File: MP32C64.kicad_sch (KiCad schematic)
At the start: 15 parts, among them CN2 C64_CASS_PORT, J1 Conn_Coaxial, SW1 SW_SPDT, U1 4069

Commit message: Almost ready
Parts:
- removed J1: Conn_Coaxial, symbol Connector:Conn_Coaxial
- added CN1: AUDIO_IN, MP32C64:SWITCHCRAFT_PJRAN1X1U01X, symbol PJRAN1X1U01X:PJRAN1X1U01X
- R1, R2, R3, R4, R5, R6, R7, R8: footprint Resistor_THT:R_Axial_DIN0207_L6.3mm_D2.5mm_P7.62mm_Horizontal -> Resistor_THT:R_Axial_DIN0207_L6.3mm_D2.5mm_P10.16mm_Horizontal
- SW1: value SW_SPDT -> SW_INVERT
- U1: value 4069 -> CD4069
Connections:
- net GND: now also CN1.1
- net at C1.1, R1.2: now also CN1.2
- no-connect marks 1 -> 2
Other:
- moved on the sheet: C1, R1

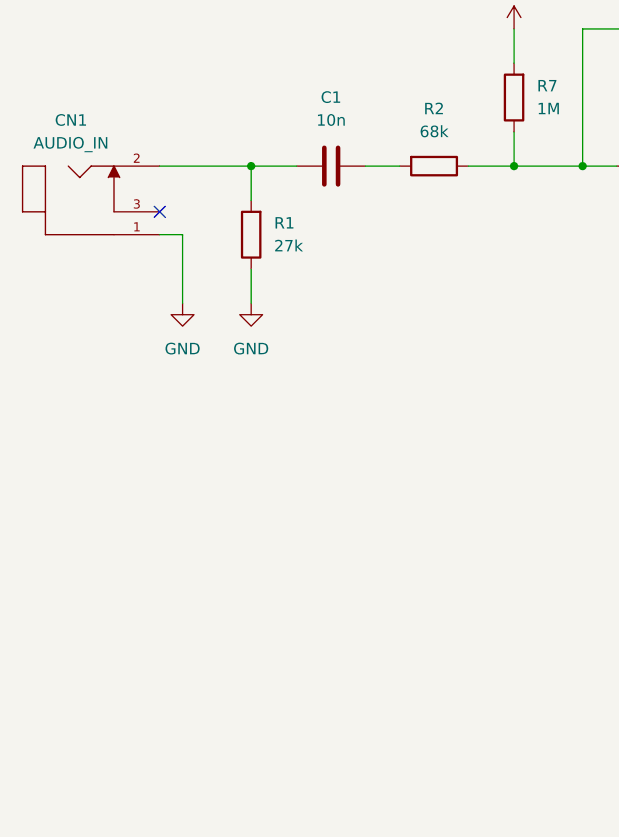
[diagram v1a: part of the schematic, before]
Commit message: Add dual support for RCA/3.5" jack connector
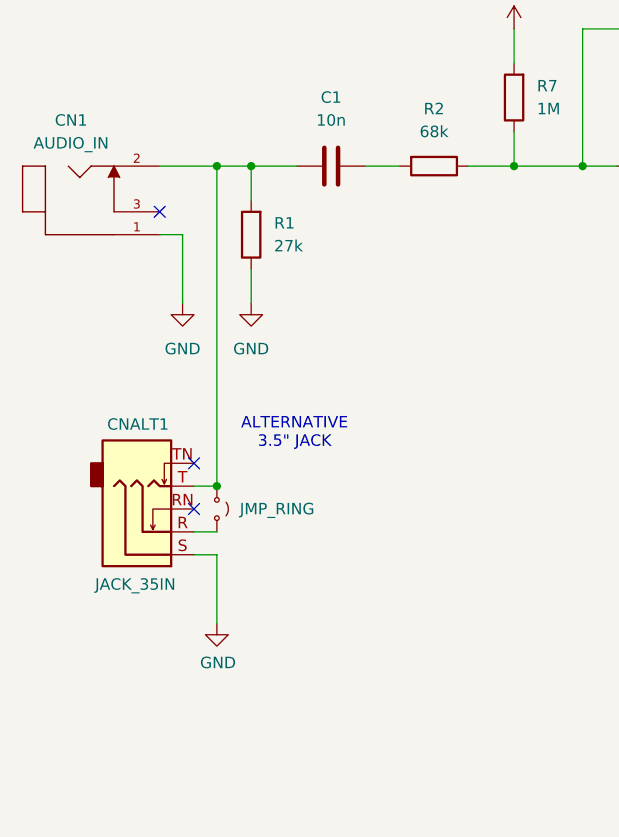
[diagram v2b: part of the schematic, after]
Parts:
- added CNALT1: JACK_35IN, MP32C64:AudioJack_SJ1-3525N, symbol Connector_Audio:AudioJack3_SwitchTR
- added JP1: JMP_RING, Jumper:SolderJumper-2_P1.3mm_Open_RoundedPad1.0x1.5mm, symbol Jumper:Jumper_2_Small_Open
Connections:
- net GND: now also CNALT1.S
- net at C1.1, CN1.2, R1.2: now also CNALT1.T, JP1.1 (A)
- new net: CNALT1.R, JP1.2 (B)
- no-connect marks 2 -> 4
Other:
- note added: "ALTERNATIVE 3.5" JACK"

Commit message: Add license, etc.
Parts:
- removed JP1: JMP_RING, Jumper:SolderJumper-2_P1.3mm_Open_RoundedPad1.0x1.5mm, symbol Jumper:Jumper_2_Small_Open
- added V0: LICENSE, MP32C64:cc_by_nc_sa_small, symbol void:Void
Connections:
- no-connect marks 4 -> 5
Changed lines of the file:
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@@
 		(company "SukkoPera")
 		(comment 1 "Audio Device to C64 Datassette Adapter")
-		(comment 2 "https://www.c64-wiki.com/wiki/MP32C64")
+		(comment 2 "https://github.com/SukkoPera/MP32C64")
 		(comment 3 "Original design by Kopsec")
 	)
@@
 	)
 	(junction
-		(at 34.29 91.44)
-		(diameter 0)
-		(color 0 0 0 0)
-	)
-	(junction
 		(at 67.31 55.88)
 		(diameter 0)
@@
 	)
 	(no_connect
+		(at 31.75 96.52)
+	)
+	(no_connect
 		(at 31.75 88.9)
 	)
@@
 		(pts
 			(xy 261.62 66.04) (xy 259.08 66.04)
-		)
-		(stroke
-			(width 0)
-			(type default)
-		)
-	)
-	(wire
-		(pts
-			(xy 31.75 96.52) (xy 34.29 96.52)
 		)
 		(stroke
@@
 	)
 	(symbol
+		(lib_id "void:Void")
+		(at 266.7 161.29 0)
+		(unit 1)
+		(exclude_from_sim no)
+		(in_bom yes)
+		(on_board yes)
+		(dnp no)
+		(fields_autoplaced yes)
+		(property "Reference" "V0"
+			(at 269.24 160.0199 0)
+			(effects
+				(font
+					(size 1.27 1.27)
+				)
+				(justify left)
+			)
+		)
+		(property "Value" "LICENSE"
+			(at 269.24 162.5599 0)
+			(effects
+				(font
+					(size 1.27 1.27)
+				)
+				(justify left)
+			)
+		)
+		(property "Footprint" "MP32C64:cc_by_nc_sa_small"
+			(at 266.7 161.29 0)
+			(effects
+				(font
+					(size 1.27 1.27)
+				)
+				(hide yes)
+			)
+		)
+		(property "Datasheet" ""
+			(at 266.7 161.29 0)
+			(effects
+				(font
+					(size 1.27 1.27)
+				)
+				(hide yes)
+			)
+		)
+		(property "Description" ""
+			(at 266.7 161.29 0)
+			(effects
+				(font
+					(size 1.27 1.27)
+				)
+				(hide yes)
+			)
+		)
+		(instances
+			(project ""
+				(path "/1bcca956-fe5c-4556-993d-e8e650dac39a"
+					(reference "V0")
+					(unit 1)
+				)
+			)
+		)
+	)
+	(symbol
 		(lib_id "power:GND")
 		(at 250.19 69.85 0)
@@
 					(unit 1)
 				)
-			)
-		)
-	)
-	(symbol
-		(lib_id "Jumper:Jumper_2_Small_Open")
-		(at 34.29 93.98 270)
-		(unit 1)
-		(exclude_from_sim yes)
-		(in_bom yes)
-		(on_board yes)
-		(dnp no)
-		(fields_autoplaced yes)
-		(property "Reference" "JP1"
-			(at 36.83 92.7099 90)
-			(effects
-				(font
-					(size 1.27 1.27)
-				)
-				(justify left)
-				(hide yes)
-			)
-		)
-		(property "Value" "JMP_RING"
-			(at 36.83 93.9799 90)
-			(effects
-				(font
-					(size 1.27 1.27)
-				)
-				(justify left)
-			)
-		)
-		(property "Footprint" "Jumper:SolderJumper-2_P1.3mm_Open_RoundedPad1.0x1.5mm"
-			(at 34.29 93.98 0)
-			(effects
-				(font
-					(size 1.27 1.27)
-				)
-				(hide yes)
-			)
-		)
-		(property "Datasheet" "~"
-			(at 34.29 93.98 0)
-			(effects
-				(font
-					(size 1.27 1.27)
-				)
-				(hide yes)
-			)
-		)
-		(property "Description" "Jumper, 2-pole, small symbol, open"
-			(at 34.29 93.98 0)
-			(effects
-				(font
-					(size 1.27 1.27)
-				)
-				(hide yes)
-			)
-		)
-		(pin "1"
-		)
-		(pin "2"
-		)
-		(instances
-			(project ""
-				(path "/1bcca956-fe5c-4556-993d-e8e650dac39a"
-					(reference "JP1")
-					(unit 1)
-				)

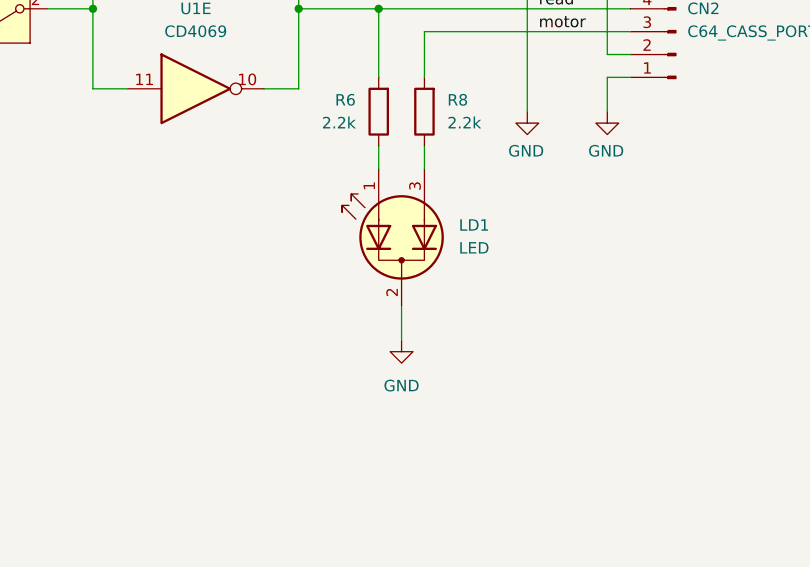
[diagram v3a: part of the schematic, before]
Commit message: Replace dual LED with 2 separate LEDs
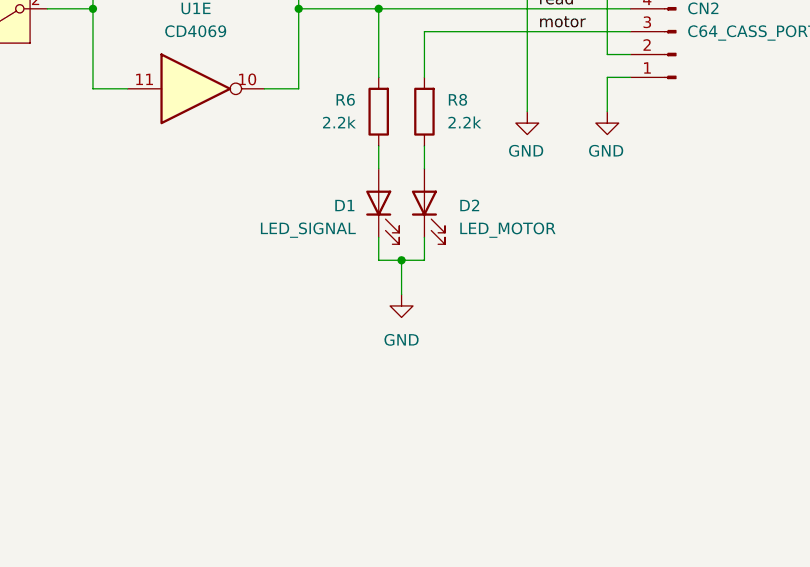
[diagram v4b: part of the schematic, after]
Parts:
- removed LD1: LED, LED_THT:LED_D3.0mm-3, symbol Device:LED_Dual_AKA
- added D1: LED_SIGNAL, LED_THT:LED_D3.0mm, symbol Device:LED
- added D2: LED_MOTOR, LED_THT:LED_D3.0mm, symbol Device:LED
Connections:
- net GND: now also D1.1 (K), D2.1 (K)
- net at R8.1: now also D2.2 (A)
- net at R6.1: now also D1.2 (A)
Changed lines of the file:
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@@
 	(title_block
 		(title "MP32C64")
-		(date "2025-02-06")
+		(date "2025-03-17")
 		(rev "1git")
 		(company "SukkoPera")
@@
 	)
 	(junction
+		(at 236.22 86.36)
+		(diameter 0)
+		(color 0 0 0 0)
+	)
+	(junction
 		(at 201.93 58.42)
 		(diameter 0)
@@
 	(wire
 		(pts
+			(xy 233.68 83.82) (xy 233.68 86.36)
+		)
+		(stroke
+			(width 0)
+			(type default)
+		)
+	)
+	(wire
+		(pts
 			(xy 67.31 55.88) (xy 67.31 52.07)
 		)
@@
 	(wire
 		(pts
-			(xy 236.22 91.44) (xy 236.22 95.25)
+			(xy 236.22 86.36) (xy 236.22 90.17)
 		)
 		(stroke
@@
 	(wire
 		(pts
+			(xy 233.68 86.36) (xy 236.22 86.36)
+		)
+		(stroke
+			(width 0)
+			(type default)
+		)
+	)
+	(wire
+		(pts
+			(xy 238.76 86.36) (xy 238.76 83.82)
+		)
+		(stroke
+			(width 0)
+			(type default)
+		)
+	)
+	(wire
+		(pts
 			(xy 38.1 55.88) (xy 38.1 59.69)
 		)
@@
 	(wire
 		(pts
+			(xy 236.22 86.36) (xy 238.76 86.36)
+		)
+		(stroke
+			(width 0)
+			(type default)
+		)
+	)
+	(wire
+		(pts
 			(xy 201.93 67.31) (xy 205.74 67.31)
 		)
@@
 	)
 	(symbol
+		(lib_id "Device:LED")
+		(at 233.68 80.01 90)
+		(unit 1)
+		(exclude_from_sim no)
+		(in_bom yes)
+		(on_board yes)
+		(dnp no)
+		(fields_autoplaced yes)
+		(property "Reference" "D1"
+			(at 231.14 80.3274 90)
+			(effects
+				(font
+					(size 1.27 1.27)
+				)
+				(justify left)
+			)
+		)
+		(property "Value" "LED_SIGNAL"
+			(at 231.14 82.8674 90)
+			(effects
+				(font
+					(size 1.27 1.27)
+				)
+				(justify left)
+			)
+		)
+		(property "Footprint" "LED_THT:LED_D3.0mm"
+			(at 233.68 80.01 0)
+			(effects
+				(font
+					(size 1.27 1.27)
+				)
+				(hide yes)
+			)
+		)
+		(property "Datasheet" "~"
+			(at 233.68 80.01 0)
+			(effects
+				(font
+					(size 1.27 1.27)
+				)
+				(hide yes)
+			)
+		)
+		(property "Description" "Light emitting diode"
+			(at 233.68 80.01 0)
+			(effects
+				(font
+					(size 1.27 1.27)
+				)
+				(hide yes)
+			)
+		)
+		(pin "1"
+		)
+		(pin "2"
+		)
+		(instances
+			(project ""
+				(path "/1bcca956-fe5c-4556-993d-e8e650dac39a"
+					(reference "D1")
+					(unit 1)
+				)
+			)
+		)
+	)
+	(symbol
 		(lib_id "power:GND")
 		(at 34.29 106.68 0)
@@
 	)
 	(symbol
+		(lib_id "Device:LED")
+		(at 238.76 80.01 90)
+		(unit 1)
+		(exclude_from_sim no)
+		(in_bom yes)
+		(on_board yes)
+		(dnp no)
+		(fields_autoplaced yes)
+		(property "Reference" "D2"
+			(at 242.57 80.3274 90)
+			(effects
+				(font
+					(size 1.27 1.27)
+				)
+				(justify right)
+			)
+		)
+		(property "Value" "LED_MOTOR"
+			(at 242.57 82.8674 90)
+			(effects
+				(font
+					(size 1.27 1.27)
+				)
+				(justify right)
+			)
+		)
+		(property "Footprint" "LED_THT:LED_D3.0mm"
+			(at 238.76 80.01 0)
+			(effects
+				(font
+					(size 1.27 1.27)
+				)
+				(hide yes)
+			)
+		)
+		(property "Datasheet" "~"
+			(at 238.76 80.01 0)
+			(effects
+				(font
+					(size 1.27 1.27)
+				)
+				(hide yes)
+			)
+		)
+		(property "Description" "Light emitting diode"
+			(at 238.76 80.01 0)
+			(effects
+				(font
+					(size 1.27 1.27)
+				)
+				(hide yes)
+			)
+		)
+		(pin "1"
+		)
+		(pin "2"
+		)
+		(instances
+			(project "MP32C64"
+				(path "/1bcca956-fe5c-4556-993d-e8e650dac39a"
+					(reference "D2")
+					(unit 1)
+				)
+			)
+		)
+	)
+	(symbol
 		(lib_id "power:GND")
 		(at 30.48 71.12 0)
@@
 	)
 	(symbol
-		(lib_id "Device:LED_Dual_AKA")
-		(at 236.22 83.82 90)
-		(unit 1)
-		(exclude_from_sim no)
-		(in_bom yes)
-		(on_board yes)
-		(dnp no)
-		(fields_autoplaced yes)
-		(property "Reference" "LD1"
-			(at 242.57 82.4864 90)
-			(effects
-				(font
-					(size 1.27 1.27)
-				)
-				(justify right)
-			)
-		)
-		(property "Value" "LED"
-			(at 242.57 85.0264 90)
-			(effects
-				(font
-					(size 1.27 1.27)
-				)
-				(justify right)
-			)
-		)
-		(property "Footprint" "LED_THT:LED_D3.0mm-3"
-			(at 236.22 83.82 0)
-			(effects
-				(font
-					(size 1.27 1.27)
-				)
-				(hide yes)
-			)
-		)
-		(property "Datasheet" "~"
-			(at 236.22 83.82 0)
-			(effects
-				(font
-					(size 1.27 1.27)
-				)
-				(hide yes)
-			)
-		)
-		(property "Description" "Dual LED, common cathode on pin 2"
-			(at 236.22 83.82 0)
-			(effects
-				(font
-					(size 1.27 1.27)
-				)
-				(hide yes)
-			)
-		)
-		(pin "1"
-		)
-		(pin "2"
-		)
-		(pin "3"
-		)
-		(instances
-			(project ""
-				(path "/1bcca956-fe5c-4556-993d-e8e650dac39a"
-					(reference "LD1")
-					(unit 1)
-				)
-			)
-		)
-	)
-	(symbol
 		(lib_id "Device:C")
 		(at 26.67 168.91 180)
@@
 	(symbol
 		(lib_id "power:GND")
-		(at 236.22 95.25 0)
+		(at 236.22 90.17 0)
 		(unit 1)
 		(exclude_from_sim no)
@@
 		(fields_autoplaced yes)
 		(property "Reference" "#PWR09"
-			(at 236.22 101.6 0)
+			(at 236.22 96.52 0)
 			(effects
 				(font
@@
 		)
 		(property "Value" "GND"
-			(at 236.22 100.33 0)
+			(at 236.22 95.25 0)
 			(effects
 				(font
@@
 		)
 		(property "Footprint" ""
-			(at 236.22 95.25 0)
+			(at 236.22 90.17 0)
 			(effects
 				(font
@@
 		)
 		(property "Datasheet" ""
-			(at 236.22 95.25 0)
+			(at 236.22 90.17 0)
 			(effects
 				(font
@@
 		)
 		(property "Description" "Power symbol creates a global label with name \"GND\" , ground"
-			(at 236.22 95.25 0)
+			(at 236.22 90.17 0)
 			(effects
 				(font

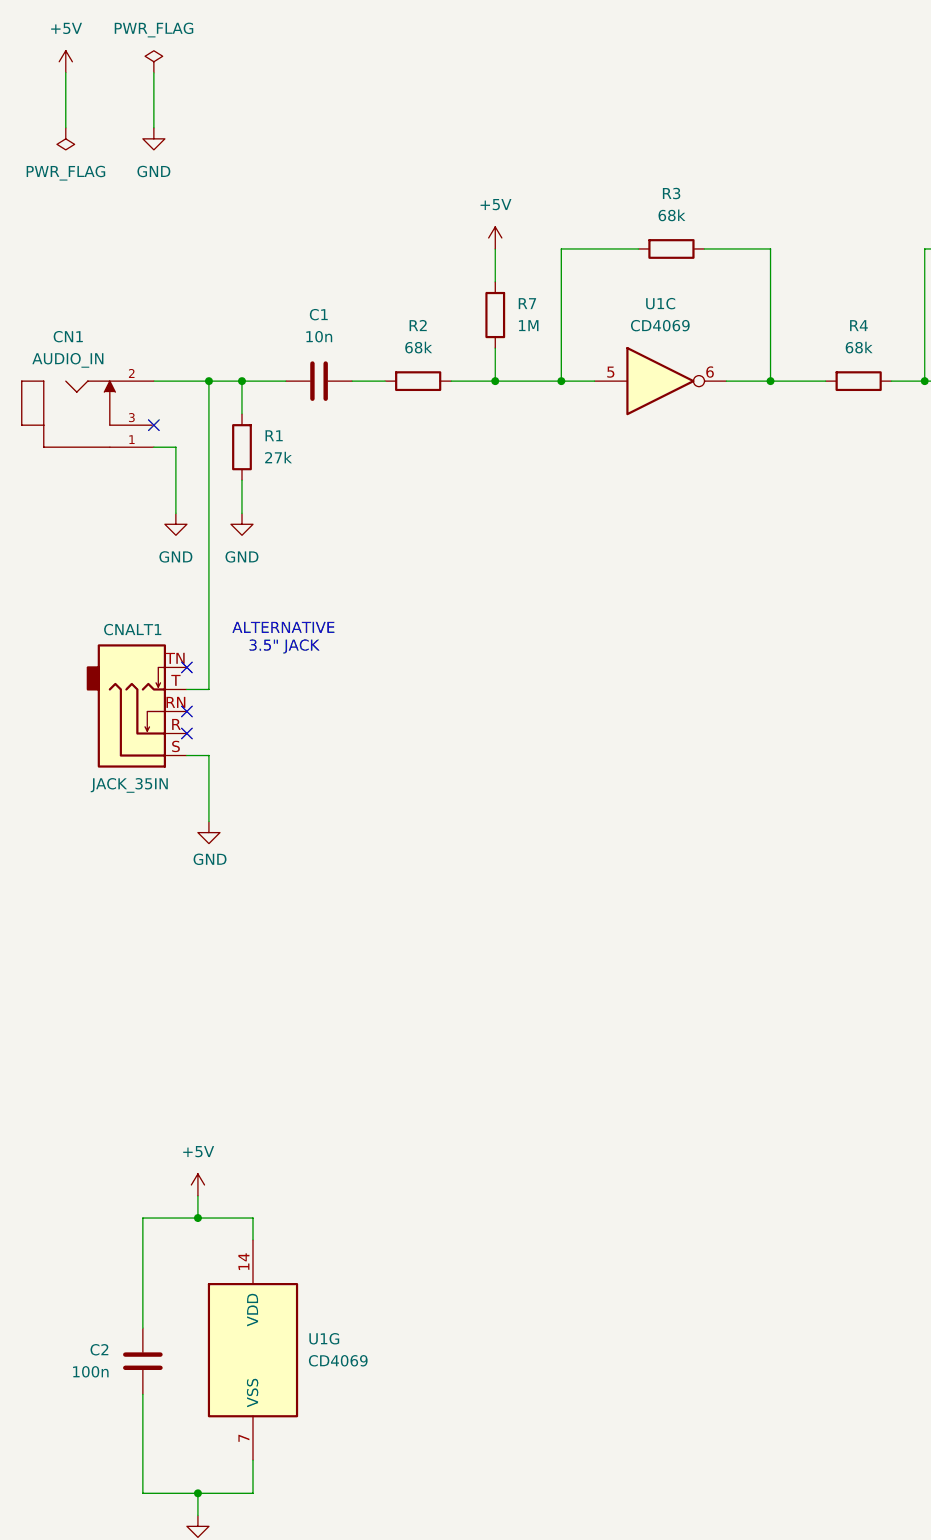
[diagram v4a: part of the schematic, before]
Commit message: Add C2, found in some other schematics
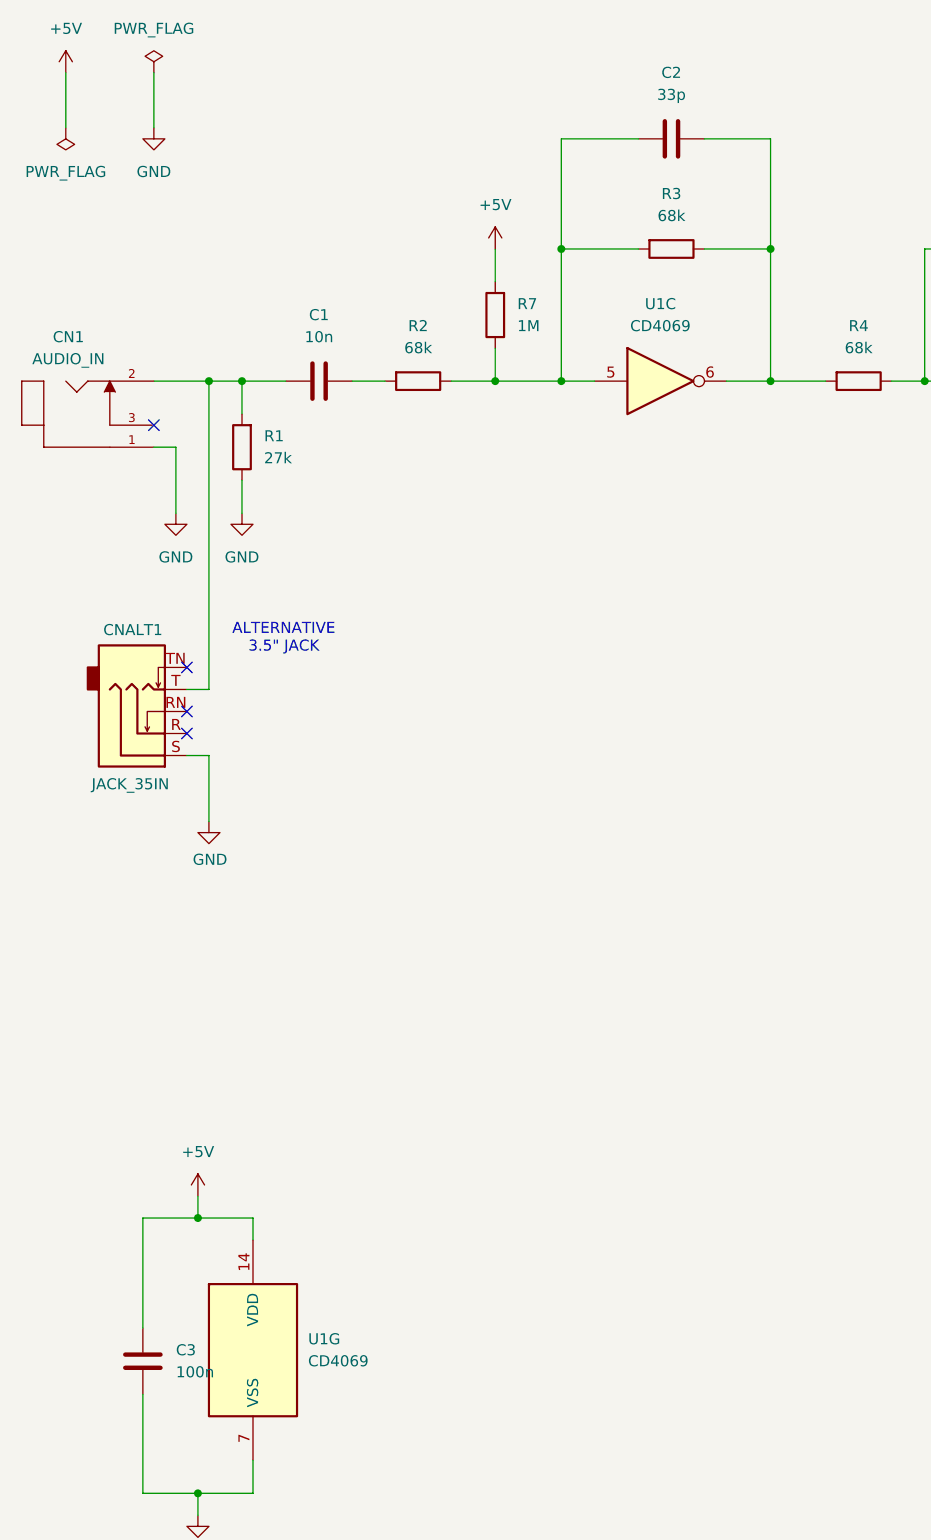
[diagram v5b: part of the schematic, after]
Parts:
- added C2: 33p, Capacitor_THT:C_Disc_D7.0mm_W2.5mm_P5.00mm, symbol Device:C
- renumbered C2 to C3
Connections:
- net at R3.1, R4.2, U1.6: now also C2.2
- net at R2.1, R3.2, R7.1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: now also C2.1
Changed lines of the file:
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@@
 	(title_block
 		(title "MP32C64")
-		(date "2025-03-17")
+		(date "2025-03-25")
 		(rev "1git")
 		(company "SukkoPera")
@@
 	)
 	(junction
+		(at 99.06 40.64)
+		(diameter 0)
+		(color 0 0 0 0)
+	)
+	(junction
+		(at 74.93 40.64)
+		(diameter 0)
+		(color 0 0 0 0)
+	)
+	(junction
 		(at 233.68 58.42)
 		(diameter 0)
@@
 	(wire
 		(pts
+			(xy 91.44 27.94) (xy 99.06 27.94)
+		)
+		(stroke
+			(width 0)
+			(type default)
+		)
+	)
+	(wire
+		(pts
 			(xy 158.75 40.64) (xy 158.75 55.88)
 		)
@@
 	(wire
 		(pts
+			(xy 74.93 27.94) (xy 83.82 27.94)
+		)
+		(stroke
+			(width 0)
+			(type default)
+		)
+	)
+	(wire
+		(pts
+			(xy 74.93 40.64) (xy 74.93 27.94)
+		)
+		(stroke
+			(width 0)
+			(type default)
+		)
+	)
+	(wire
+		(pts
 			(xy 17.78 20.32) (xy 17.78 26.67)
 		)
@@
 	(wire
 		(pts
+			(xy 99.06 27.94) (xy 99.06 40.64)
+		)
+		(stroke
+			(width 0)
+			(type default)
+		)
+	)
+	(wire
+		(pts
 			(xy 224.79 58.42) (xy 224.79 67.31)
 		)
@@
 	)
 	(symbol
+		(lib_id "Device:C")
+		(at 87.63 27.94 90)
+		(unit 1)
+		(exclude_from_sim no)
+		(in_bom yes)
+		(on_board yes)
+		(dnp no)
+		(fields_autoplaced yes)
+		(property "Reference" "C2"
+			(at 87.63 20.32 90)
+			(effects
+				(font
+					(size 1.27 1.27)
+				)
+			)
+		)
+		(property "Value" "33p"
+			(at 87.63 22.86 90)
+			(effects
+				(font
+					(size 1.27 1.27)
+				)
+			)
+		)
+		(property "Footprint" "Capacitor_THT:C_Disc_D7.0mm_W2.5mm_P5.00mm"
+			(at 91.44 26.9748 0)
+			(effects
+				(font
+					(size 1.27 1.27)
+				)
+				(hide yes)
+			)
+		)
+		(property "Datasheet" "~"
+			(at 87.63 27.94 0)
+			(effects
+				(font
+					(size 1.27 1.27)
+				)
+				(hide yes)
+			)
+		)
+		(property "Description" "Unpolarized capacitor"
+			(at 87.63 27.94 0)
+			(effects
+				(font
+					(size 1.27 1.27)
+				)
+				(hide yes)
+			)
+		)
+		(pin "1"
+		)
+		(pin "2"
+		)
+		(instances
+			(project "MP32C64"
+				(path "/1bcca956-fe5c-4556-993d-e8e650dac39a"
+					(reference "C2")
+					(unit 1)
+				)
+			)
+		)
+	)
+	(symbol
 		(lib_id "Device:R")
 		(at 233.68 69.85 180)
@@
 		(dnp no)
 		(fields_autoplaced yes)
-		(property "Reference" "C2"
-			(at 22.86 167.6399 0)
+		(property "Reference" "C3"
+			(at 30.48 167.6399 0)
 			(effects
 				(font
 					(size 1.27 1.27)
 				)
-				(justify left)
+				(justify right)
 			)
 		)
 		(property "Value" "100n"
-			(at 22.86 170.1799 0)
+			(at 30.48 170.1799 0)
 			(effects
 				(font
 					(size 1.27 1.27)
 				)
-				(justify left)
+				(justify right)
 			)
 		)
@@
 			(project "MP32C64"
 				(path "/1bcca956-fe5c-4556-993d-e8e650dac39a"
-					(reference "C2")
+					(reference "C3")
 					(unit 1)
 				)
